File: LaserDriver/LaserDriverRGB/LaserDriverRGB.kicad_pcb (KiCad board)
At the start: 4 copper layers, 50 x 50 mm, 55 parts, among them J1 SIGNAL, J2 POWER, U3 MCP4728, U4 MCP4728, U5 MCP4728

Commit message: fixed
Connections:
- R4 pad 1: +5.5V -> 3V3
- R5 pad 2: +5.5 -> 3V3
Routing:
- net 3V3: track 107.7 -> 126.4 mm, vias 2 -> 5
- net +5.5V: track 54.2 -> 53.2 mm

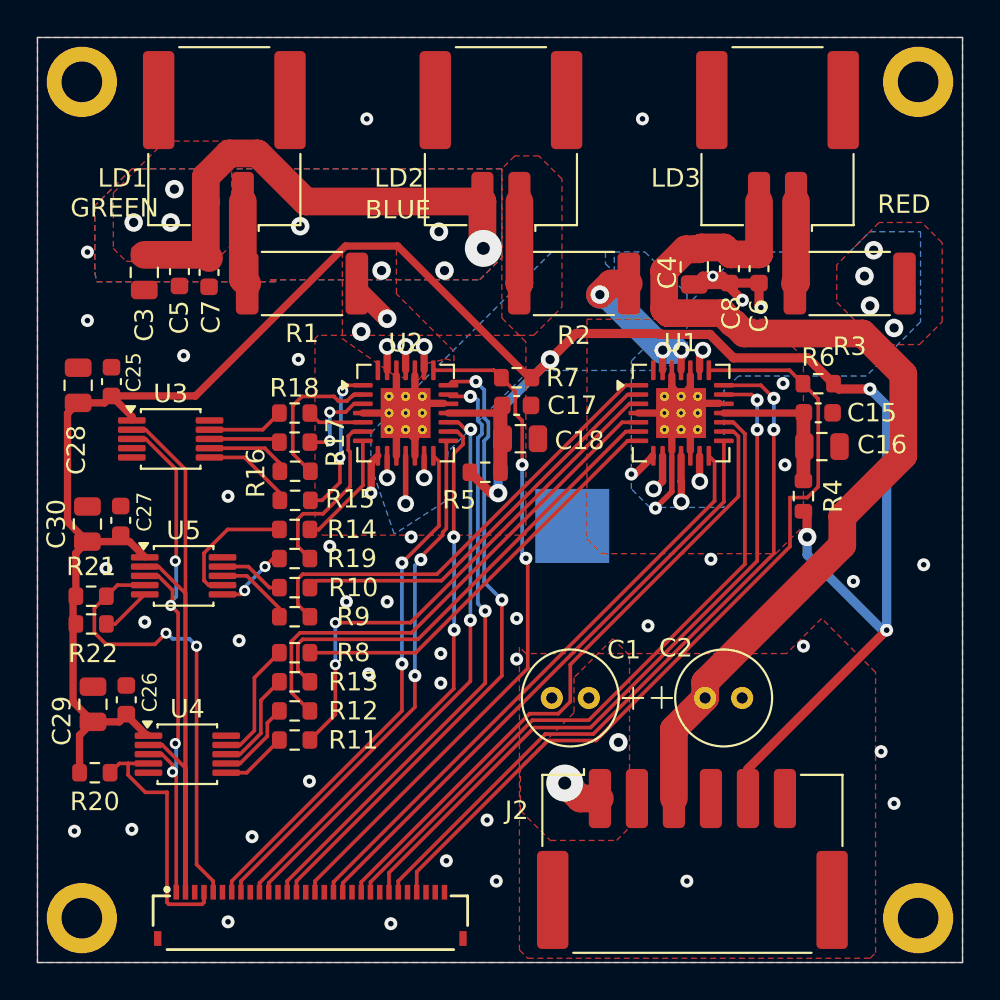
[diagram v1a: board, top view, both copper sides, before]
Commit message: rounded fillets
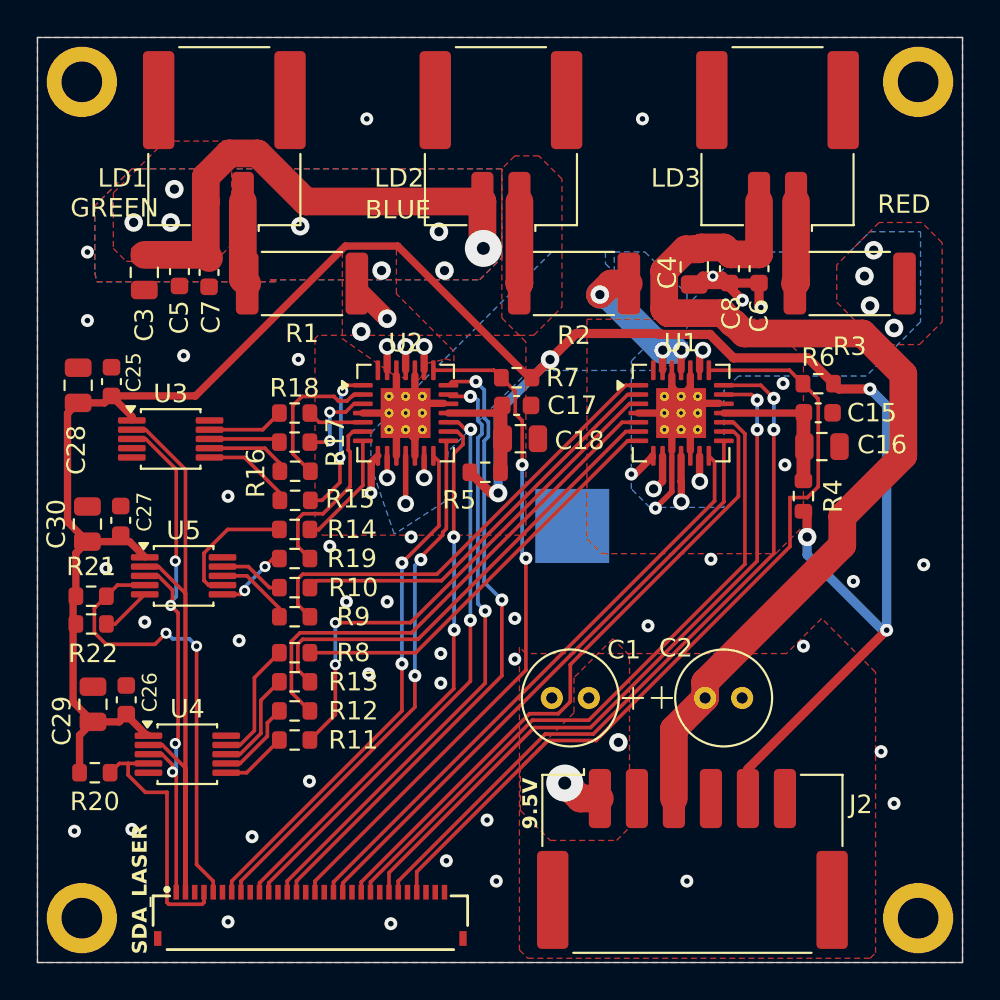
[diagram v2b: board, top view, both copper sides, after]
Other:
- board text added: "9.5V"
- board text added: "SDA_LASER"
